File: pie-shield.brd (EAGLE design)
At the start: 35.5 x 56.2 mm, 15 parts, among them IC6 78L05, IC8 MAX487, X6 RJ45-8L-B

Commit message: before wiring to raspberry
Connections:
- net N$35 renamed SELECT
- net +5V: now also U$2.P1_2, U$2.P1_4, U$2.P5_1
- net GND: now also U$2.P1_14, U$2.P1_20, U$2.P1_6, U$2.P5_7, U$2.P5_8
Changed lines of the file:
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@@
 <contactref element="R22" pad="1"/>
 <contactref element="R19" pad="1"/>
-<wire x1="25.3475" y1="38.1" x2="33.92" y2="40.64" width="0" layer="19" extent="1-1"/>
-<wire x1="28.575" y1="34.8234" x2="25.3475" y2="38.1" width="0" layer="19" extent="1-1"/>
-<wire x1="29.845" y1="34.8234" x2="28.575" y2="34.8234" width="0" layer="19" extent="1-1"/>
+<contactref element="U$2" pad="P1_2"/>
+<contactref element="U$2" pad="P1_4"/>
+<contactref element="U$2" pad="P5_1"/>
+<wire x1="29.845" y1="34.8234" x2="33.92" y2="40.64" width="0" layer="19" extent="1-1"/>
+<wire x1="28.575" y1="34.8234" x2="29.845" y2="34.8234" width="0" layer="19" extent="1-1"/>
+<wire x1="25.3475" y1="38.1" x2="28.575" y2="34.8234" width="0" layer="19" extent="1-1"/>
 <wire x1="17.7275" y1="38.1" x2="25.3475" y2="38.1" width="0" layer="19" extent="1-1"/>
+<wire x1="7.62" y1="48.26" x2="17.7275" y2="38.1" width="0" layer="19" extent="1-1"/>
+<wire x1="5.08" y1="53.34" x2="7.62" y2="48.26" width="0" layer="19" extent="1-1"/>
+<wire x1="2.54" y1="53.34" x2="5.08" y2="53.34" width="0" layer="19" extent="1-1"/>
 </signal>
-<signal name="N$35">
+<signal name="SELECT">
 <contactref element="OK3" pad="3"/>
 </signal>
@@
 <contactref element="OK2" pad="5"/>
 <contactref element="C24" pad="1"/>
+<contactref element="U$2" pad="P1_14"/>
+<contactref element="U$2" pad="P1_20"/>
+<contactref element="U$2" pad="P5_8"/>
+<contactref element="U$2" pad="P5_7"/>
+<contactref element="U$2" pad="P1_6"/>
+<wire x1="17.78" y1="53.34" x2="25.4" y2="53.34" width="0" layer="19" extent="1-1"/>
+<wire x1="15.24" y1="48.26" x2="17.78" y2="53.34" width="0" layer="19" extent="1-1"/>
+<wire x1="15.24" y1="45.72" x2="15.24" y2="48.26" width="0" layer="19" extent="1-1"/>
+<wire x1="7.62" y1="53.34" x2="15.24" y2="48.26" width="0" layer="19" extent="1-1"/>
+<wire x1="32.12" y1="40.64" x2="25.4" y2="53.34" width="0" layer="19" extent="1-1"/>
+<wire x1="32.385" y1="34.8234" x2="32.12" y2="40.64" width="0" layer="19" extent="1-1"/>
 </signal>
 </signals>

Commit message: wired
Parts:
- moved C24 5.40 mm to (28.3, 38.1)
- moved R19 0.63 mm to (16.8, 37.5)
- moved R22 0.45 mm to (24.1, 38.4)
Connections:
- net RXD_AL: now also U$2.P5_5
- net SELECT: now also U$2.P5_6
- net TXD_AL: now also U$2.P5_4
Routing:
- net +5V: track 0.00 -> 46.6 mm, vias 0 -> 3
- net RXD_AL: track 0.00 -> 26.3 mm
- net SELECT: track 0.00 -> 14.8 mm
- net TXD_AL: track 0.00 -> 12.7 mm
- net N$44: track 0.00 -> 3.70 mm
- net N$32: track 0.00 -> 2.66 mm
- net TXD1: track 21.3 -> 22.4 mm
- net RXD1: track 20.3 -> 21.4 mm

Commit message: 1 layered
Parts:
- moved C24 0.71 mm to (27.6, 37.8)
- moved R22 0.71 mm to (24.4, 37.8)
- moved IC6 0.64 mm to (31.1, 6.35)
- moved C16 0.45 mm to (27.6, 2.54)
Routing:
- net +5V1: track 57.7 -> 62.8 mm
- net +24V: track 18.5 -> 20.8 mm, vias 1 -> 2
- net +5V: track 46.6 -> 48.8 mm
- net N$44: track 3.70 -> 2.98 mm

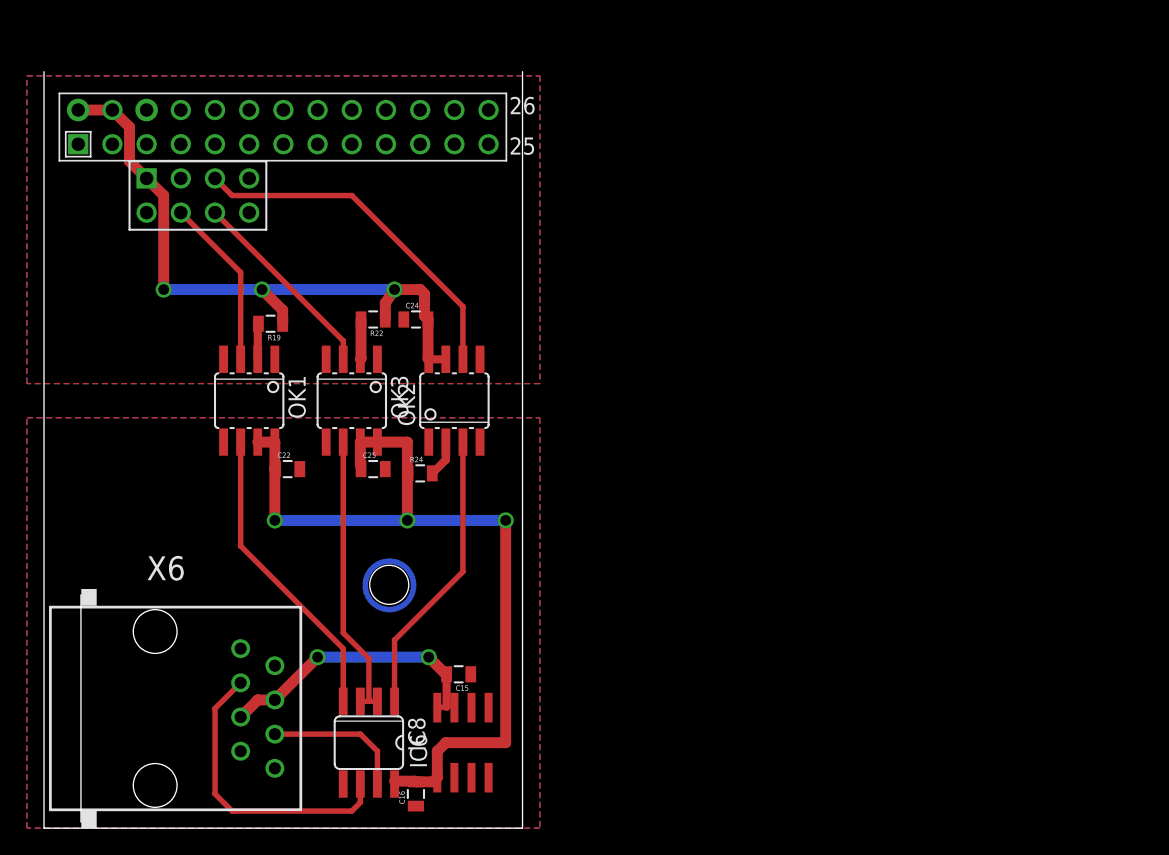
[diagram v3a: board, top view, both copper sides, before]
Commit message: one-layerd with ground-bridges
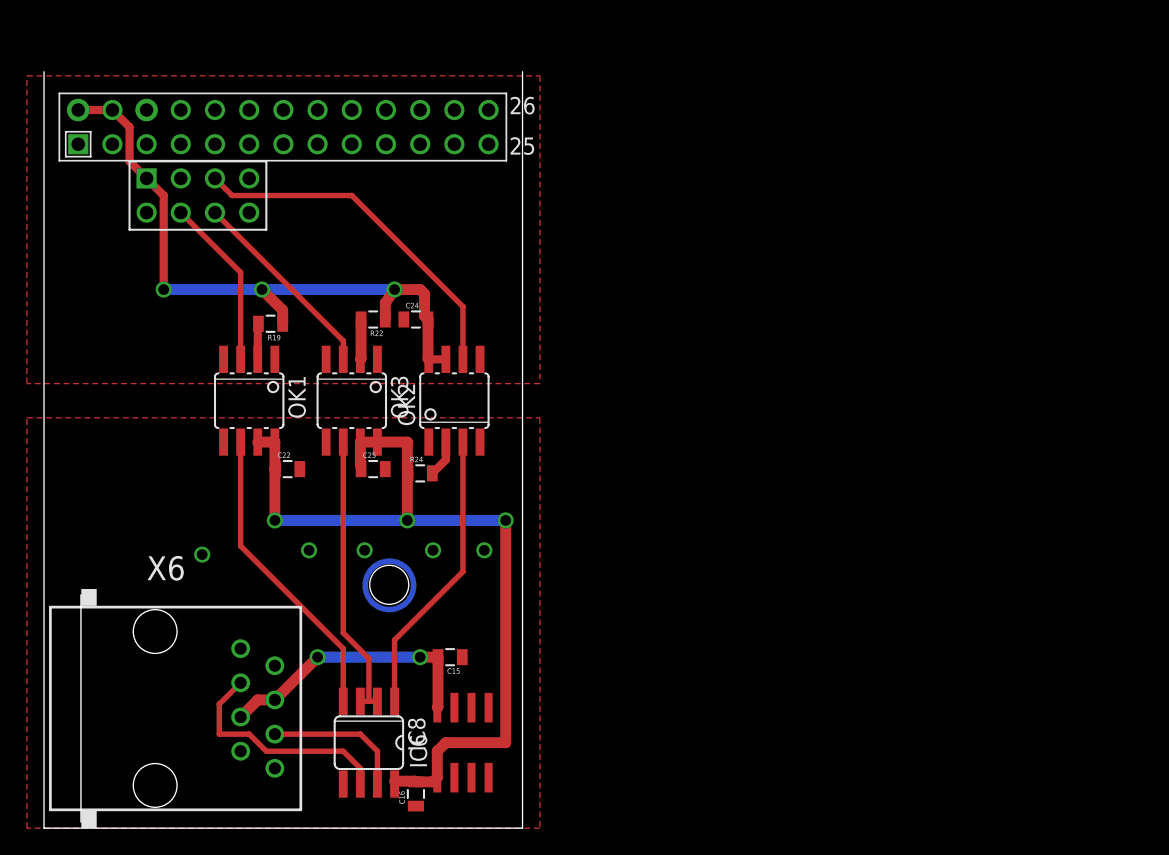
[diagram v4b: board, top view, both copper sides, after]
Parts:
- moved C15 1.42 mm to (30.2, 12.7)
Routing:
- net A1: track 22.0 -> 17.2 mm
- net +24V: track 20.8 -> 20.3 mm
- removed copper zone on layer 16, net GND
- removed copper zone on layer 16, net GND_AL
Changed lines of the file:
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@@
 </class>
 </classes>
-<designrules name="default">
+<designrules name="LaenPCBOrder">
 <description language="de">&lt;b&gt;EAGLE Design Rules&lt;/b&gt;
 &lt;p&gt;
@@
 Einstellungen hier und speichern die Design Rules unter
 einem neuen Namen ab.</description>
-<description language="en">&lt;b&gt;EAGLE Design Rules&lt;/b&gt;
+<description language="en">&lt;b&gt;Laen's PCB Order Design Rules&lt;/b&gt;
 &lt;p&gt;
-The default Design Rules have been set to cover
-a wide range of applications. Your particular design
-may have different requirements, so please make the
-necessary adjustments and save your customized
-design rules under a new name.</description>
+Please make sure your boards conform to these design rules.</description>
 <param name="layerSetup" value="(1*16)"/>
-<param name="mtCopper" value="0.035mm 0.035mm 0.035mm 0.035mm 0.035mm 0.035mm 0.035mm 0.035mm 0.035mm 0.035mm 0.035mm 0.035mm 0.035mm 0.035mm 0.035mm 0.035mm"/>
-<param name="mtIsolate" value="1.5mm 0.15mm 0.2mm 0.15mm 0.2mm 0.15mm 0.2mm 0.15mm 0.2mm 0.15mm 0.2mm 0.15mm 0.2mm 0.15mm 0.2mm"/>
-<param name="mdWireWire" value="8mil"/>
-<param name="mdWirePad" value="8mil"/>
-<param name="mdWireVia" value="8mil"/>
-<param name="mdPadPad" value="8mil"/>
-<param name="mdPadVia" value="8mil"/>
-<param name="mdViaVia" value="8mil"/>
-<param name="mdSmdPad" value="8mil"/>
-<param name="mdSmdVia" value="8mil"/>
-<param name="mdSmdSmd" value="8mil"/>
+<param name="mtCopper" value="0.0356mm 0.0356mm 0.0356mm 0.0356mm 0.0356mm 0.0356mm 0.0356mm 0.0356mm 0.0356mm 0.0356mm 0.0356mm 0.0356mm 0.0356mm 0.0356mm 0.0356mm 0.0356mm"/>
+<param name="mtIsolate" value="1.5011mm 0.1499mm 0.2007mm 0.1499mm 0.2007mm 0.1499mm 0.2007mm 0.1499mm 0.2007mm 0.1499mm 0.2007mm 0.1499mm 0.2007mm 0.1499mm 0.2007mm"/>
+<param name="mdWireWire" value="6mil"/>
+<param name="mdWirePad" value="6mil"/>
+<param name="mdWireVia" value="6mil"/>
+<param name="mdPadPad" value="6mil"/>
+<param name="mdPadVia" value="6mil"/>
+<param name="mdViaVia" value="6mil"/>
+<param name="mdSmdPad" value="6mil"/>
+<param name="mdSmdVia" value="6mil"/>
+<param name="mdSmdSmd" value="6mil"/>
 <param name="mdViaViaSameLayer" value="8mil"/>
 <param name="mnLayersViaInSmd" value="2"/>
-<param name="mdCopperDimension" value="40mil"/>
-<param name="mdDrill" value="8mil"/>
+<param name="mdCopperDimension" value="15mil"/>
+<param name="mdDrill" value="6mil"/>
 <param name="mdSmdStop" value="0mil"/>
-<param name="msWidth" value="10mil"/>
-<param name="msDrill" value="24mil"/>
-<param name="msMicroVia" value="9.99mm"/>
+<param name="msWidth" value="6mil"/>
+<param name="msDrill" value="13mil"/>
+<param name="msMicroVia" value="13mil"/>
 <param name="msBlindViaRatio" value="0.5"/>
 <param name="rvPadTop" value="0.25"/>
@@
 <param name="rvMicroViaOuter" value="0.25"/>
 <param name="rvMicroViaInner" value="0.25"/>
-<param name="rlMinPadTop" value="10mil"/>
+<param name="rlMinPadTop" value="7mil"/>
 <param name="rlMaxPadTop" value="20mil"/>
-<param name="rlMinPadInner" value="10mil"/>
+<param name="rlMinPadInner" value="7mil"/>
 <param name="rlMaxPadInner" value="20mil"/>
-<param name="rlMinPadBottom" value="10mil"/>
+<param name="rlMinPadBottom" value="7mil"/>
 <param name="rlMaxPadBottom" value="20mil"/>
-<param name="rlMinViaOuter" value="8mil"/>
+<param name="rlMinViaOuter" value="7mil"/>
 <param name="rlMaxViaOuter" value="20mil"/>
-<param name="rlMinViaInner" value="8mil"/>
+<param name="rlMinViaInner" value="7mil"/>
 <param name="rlMaxViaInner" value="20mil"/>
 <param name="rlMinMicroViaOuter" value="4mil"/>
@@
 </element>
 <element name="IC6" library="linear" package="SO08" value="78L05" x="31.115" y="6.35"/>
-<element name="C15" library="SparkFun" package="0805" value="1uF" x="30.7975" y="11.43" rot="R180"/>
+<element name="C15" library="SparkFun" package="0805" value="1uF" x="30.1625" y="12.7" rot="R180"/>
 <element name="C16" library="SparkFun" package="0805" value="100nF" x="27.6225" y="2.54" rot="R90"/>
 <element name="OK1" library="optocoupler" package="SOIC08" value="HCPL0601" x="15.24" y="31.75" rot="R180">
@@
 <contactref element="C16" pad="1"/>
 <contactref element="C15" pad="1"/>
-<polygon width="0.4064" layer="16">
-<vertex x="36.83" y="0"/>
-<vertex x="-1.27" y="0"/>
-<vertex x="-1.27" y="30.48"/>
-<vertex x="36.83" y="30.48"/>
-</polygon>
 <polygon width="0.4064" layer="1">
 <vertex x="-1.27" y="30.48"/>
@@
 <vertex x="-1.27" y="0"/>
 </polygon>
+<via x="11.7475" y="20.32" extent="1-16" drill="0.8" shape="octagon"/>
+<via x="19.685" y="20.6375" extent="1-16" drill="0.8" shape="octagon"/>
+<via x="23.8125" y="20.6375" extent="1-16" drill="0.8" shape="octagon"/>
+<via x="28.8925" y="20.6375" extent="1-16" drill="0.8" shape="octagon"/>
+<via x="32.7025" y="20.6375" extent="1-16" drill="0.8" shape="octagon"/>
 </signal>
 <signal name="A1">
 <contactref element="X6" pad="3"/>
 <contactref element="IC8" pad="6"/>
-<wire x1="14.605" y1="10.795" x2="12.7" y2="8.89" width="0.4064" layer="1"/>
-<wire x1="12.7" y1="8.89" x2="12.7" y2="2.54" width="0.4064" layer="1"/>
-<wire x1="12.7" y1="2.54" x2="13.97" y2="1.27" width="0.4064" layer="1"/>
-<wire x1="13.97" y1="1.27" x2="22.86" y2="1.27" width="0.4064" layer="1"/>
-<wire x1="22.86" y1="1.27" x2="23.495" y2="1.905" width="0.4064" layer="1"/>
-<wire x1="23.495" y1="1.905" x2="23.495" y2="3.2766" width="0.4064" layer="1"/>
+<wire x1="23.495" y1="3.2766" x2="23.495" y2="4.445" width="0.4064" layer="1"/>
+<wire x1="23.495" y1="4.445" x2="22.225" y2="5.715" width="0.4064" layer="1"/>
+<wire x1="22.225" y1="5.715" x2="16.51" y2="5.715" width="0.4064" layer="1"/>
+<wire x1="16.51" y1="5.715" x2="15.24" y2="6.985" width="0.4064" layer="1"/>
+<wire x1="15.24" y1="6.985" x2="13.0175" y2="6.985" width="0.4064" layer="1"/>
+<wire x1="13.0175" y1="6.985" x2="13.0175" y2="9.2075" width="0.4064" layer="1"/>
+<wire x1="13.0175" y1="9.2075" x2="14.605" y2="10.795" width="0.4064" layer="1"/>
 </signal>
 <signal name="B1">
@@
 <wire x1="14.605" y1="8.255" x2="15.875" y2="9.525" width="0.8128" layer="1"/>
 <wire x1="15.875" y1="9.525" x2="17.145" y2="9.525" width="0.8128" layer="1"/>
-<wire x1="20.32" y1="12.7" x2="28.575" y2="12.7" width="0.8128" layer="16"/>
-<via x="28.575" y="12.7" extent="1-16" drill="0.8" shape="octagon"/>
-<wire x1="29.21" y1="8.95" x2="29.8975" y2="9.0025" width="0.4064" layer="1"/>
-<wire x1="29.8975" y1="9.0025" x2="29.8975" y2="11.43" width="0.6096" layer="1"/>
+<wire x1="20.32" y1="12.7" x2="27.94" y2="12.7" width="0.8128" layer="16"/>
+<via x="27.94" y="12.7" extent="1-16" drill="0.8" shape="octagon"/>
 <wire x1="17.145" y1="9.525" x2="20.32" y2="12.7" width="0.8128" layer="1"/>
 <via x="20.32" y="12.7" extent="1-16" drill="0.8" shape="octagon"/>
-<wire x1="28.575" y1="12.7" x2="29.845" y2="11.43" width="0.8128" layer="1"/>
-<wire x1="29.845" y1="11.43" x2="29.8975" y2="11.43" width="0.8128" layer="1"/>
+<wire x1="27.94" y1="12.7" x2="29.2625" y2="12.7" width="0.8128" layer="1"/>
+<wire x1="29.2625" y1="12.7" x2="29.2625" y2="9.0025" width="0.8128" layer="1"/>
+<wire x1="29.2625" y1="9.0025" x2="29.21" y2="8.95" width="0.8128" layer="1"/>
 </signal>
 <signal name="RXD1">
 <contactref element="OK2" pad="3"/>
 <contactref element="IC8" pad="1"/>
-<wire x1="31.115" y1="15.875" x2="31.115" y2="19.05" width="0" layer="19" extent="1-16"/>
 <wire x1="31.115" y1="19.05" x2="31.115" y2="28.6766" width="0.4064" layer="1"/>
 <wire x1="26.035" y1="9.4234" x2="26.035" y2="13.97" width="0.4064" layer="1"/>
@@
 <contactref element="U$2" pad="P1_4"/>
 <contactref element="U$2" pad="P5_1"/>
-<wire x1="2.54" y1="53.34" x2="5.08" y2="53.34" width="0.8128" layer="1"/>
-<wire x1="5.08" y1="53.34" x2="6.35" y2="52.07" width="0.8128" layer="1"/>
-<wire x1="6.35" y1="52.07" x2="6.35" y2="49.53" width="0.8128" layer="1"/>
-<wire x1="6.35" y1="49.53" x2="7.62" y2="48.26" width="0.8128" layer="1"/>
-<wire x1="7.62" y1="48.26" x2="8.89" y2="46.99" width="0.8128" layer="1"/>
+<wire x1="2.54" y1="53.34" x2="5.08" y2="53.34" width="0.6096" layer="1"/>
+<wire x1="5.08" y1="53.34" x2="6.35" y2="52.07" width="0.6096" layer="1"/>
+<wire x1="6.35" y1="52.07" x2="6.35" y2="49.53" width="0.6096" layer="1"/>
+<wire x1="6.35" y1="49.53" x2="7.62" y2="48.26" width="0.6096" layer="1"/>
+<wire x1="7.62" y1="48.26" x2="8.89" y2="46.99" width="0.6096" layer="1"/>
 <via x="26.035" y="40.005" extent="1-16" drill="0.8" shape="octagon"/>
 <wire x1="28.575" y1="34.8234" x2="29.845" y2="34.8234" width="0.6096" layer="1"/>
 <wire x1="16.1925" y1="40.005" x2="26.035" y2="40.005" width="0.8128" layer="16"/>
 <via x="16.1925" y="40.005" extent="1-16" drill="0.8" shape="octagon"/>
-<wire x1="8.89" y1="46.99" x2="8.89" y2="40.005" width="0.8128" layer="1"/>
+<wire x1="8.89" y1="46.99" x2="8.89" y2="40.005" width="0.6096" layer="1"/>
 <via x="8.89" y="40.005" extent="1-16" drill="0.8" shape="octagon"/>
 <wire x1="8.89" y1="40.005" x2="16.1925" y2="40.005" width="0.8128" layer="16"/>
@@
 </signal>
 <signal name="GND">
-<polygon width="0.4064" layer="16">
-<vertex x="-1.27" y="55.88"/>
-<vertex x="36.83" y="55.88"/>
-<vertex x="36.83" y="33.02"/>
-<vertex x="-1.27" y="33.02"/>
-</polygon>
 <polygon width="0.4064" layer="1">
 <vertex x="-1.27" y="55.88"/>
@@
 </signal>
 </signals>
+<errors>
+</errors>
 </board>
 </drawing>
